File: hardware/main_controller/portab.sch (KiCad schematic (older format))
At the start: 2 parts

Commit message: Peripherals
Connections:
- net SPI_SCK: now reaches U?.30 (PA5/ADC1_IN5/ADC2_IN5/DAC_OUT2/SPI1_SCK/TIM2_CH1/TIM2_ETR/TIM8_CH1N/USB_OTG_HS_ULPI_CK)
- net SPI_MISO: now reaches U?.31 (PA6/ADC1_IN6/ADC2_IN6/DCMI_PIXCK/SPI1_MISO/TIM13_CH1/TIM1_BKIN/TIM3_CH1/TIM8_BKIN)
- net SPI_MOSI: now reaches U?.32 (PA7/ADC1_IN7/ADC2_IN7/ETH_CRS_DV/ETH_RX_DV/SPI1_MOSI/TIM14_CH1/TIM1_CH1N/TIM3_CH2/TIM8_CH1N)
- net I2C_SCL: now reaches U?.92 (PB6/CAN2_TX/DCMI_D5/I2C1_SCL/TIM4_CH1/USART1_TX)
- net I2C_SDA: now reaches U?.93 (PB7/DCMI_VSYNC/FSMC_NL/I2C1_SDA/TIM4_CH2/USART1_RX)
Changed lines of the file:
@@
 	1    0    0    -1
 $EndComp
-Wire Wire Line
-	6100 2300 7000 2300
-Wire Wire Line
-	6100 2400 7000 2400
-Text GLabel 7000 2300 2    50   Input ~ 0
+Text GLabel 6500 2300 2    50   Input ~ 0
 STM_DM
-Text GLabel 7000 2400 2    50   Input ~ 0
+Text GLabel 6500 2400 2    50   Input ~ 0
 STM_DP
 $Comp
@@
 Text GLabel 6800 3450 2    50   Input ~ 0
 BOOT1
+Wire Wire Line
+	6300 3850 6800 3850
+Wire Wire Line
+	6300 3950 6800 3950
+Text GLabel 6800 3850 2    50   Input ~ 0
+I2C_SCL
+Text GLabel 6800 3950 2    50   Input ~ 0
+I2C_SDA
+Wire Wire Line
+	6100 1700 6500 1700
+Wire Wire Line
+	6100 1800 6500 1800
+Wire Wire Line
+	6500 1900 6100 1900
+Text GLabel 6500 1700 2    50   Input ~ 0
+SPI_SCK
+Text GLabel 6500 1800 2    50   Input ~ 0
+SPI_MISO
+Text GLabel 6500 1900 2    50   Input ~ 0
+SPI_MOSI
+Wire Wire Line
+	6500 2300 6100 2300
+Wire Wire Line
+	6100 2400 6500 2400
 $EndSCHEMATC

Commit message: LEDs
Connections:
- net LED1: now reaches U?.23 (PA0-WKUP/ADC1_IN0/ADC2_IN0/ADC3_IN0/ETH_CRS/SYS_WKUP/TIM2_CH1/TIM2_ETR/TIM5_CH1/TIM8_ETR/UART4_TX/USART2_CTS)
- net LED2: now reaches U?.24 (PA1/ADC1_IN1/ADC2_IN1/ADC3_IN1/ETH_REF_CLK/ETH_RX_CLK/TIM2_CH2/TIM5_CH2/UART4_RX/USART2_RTS)
- net LED3: now reaches U?.25 (PA2/ADC1_IN2/ADC2_IN2/ADC3_IN2/ETH_MDIO/TIM2_CH3/TIM5_CH3/TIM9_CH1/USART2_TX)
- net LED4: now reaches U?.26 (PA3/ADC1_IN3/ADC2_IN3/ADC3_IN3/ETH_COL/TIM2_CH4/TIM5_CH4/TIM9_CH2/USART2_RX/USB_OTG_HS_ULPI_D0)
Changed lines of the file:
@@
 Wire Wire Line
 	6100 2400 6500 2400
+Wire Wire Line
+	6100 1200 6500 1200
+Wire Wire Line
+	6100 1300 6500 1300
+Wire Wire Line
+	6100 1400 6500 1400
+Wire Wire Line
+	6100 1500 6500 1500
+Text GLabel 6500 1200 2    50   Input ~ 0
+LED1
+Text GLabel 6500 1300 2    50   Input ~ 0
+LED2
+Text GLabel 6500 1400 2    50   Input ~ 0
+LED3
+Text GLabel 6500 1500 2    50   Input ~ 0
+LED4
 $EndSCHEMATC

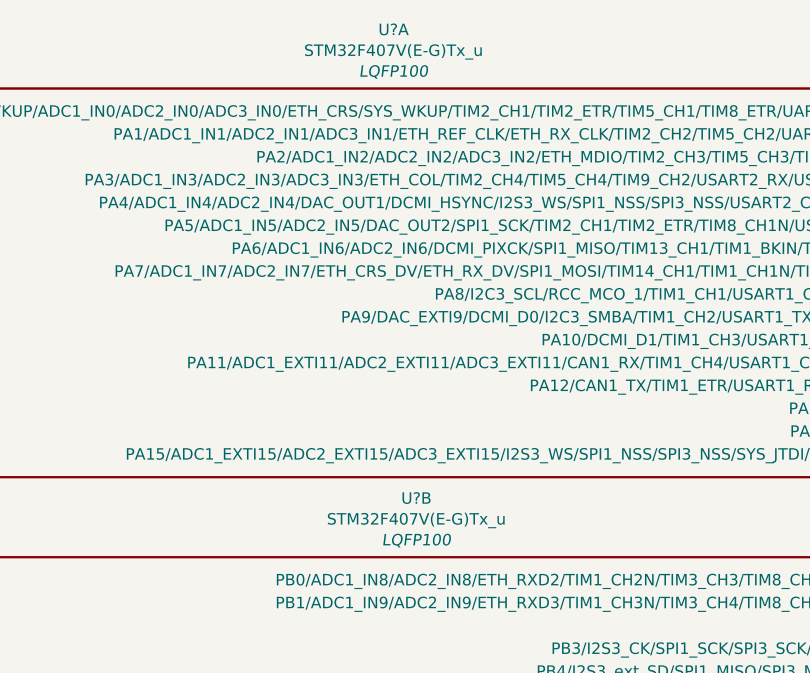
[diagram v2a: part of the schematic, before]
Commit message: Assigned names
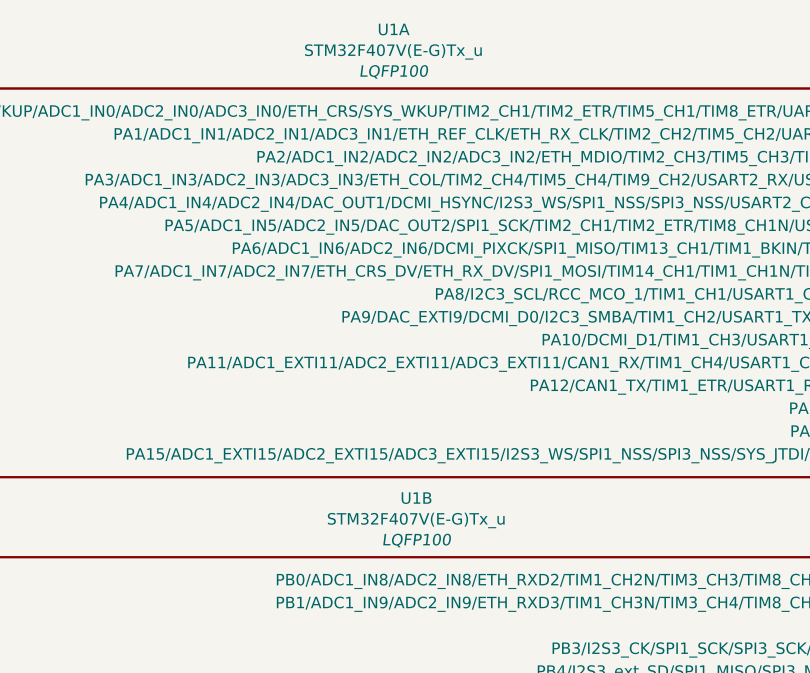
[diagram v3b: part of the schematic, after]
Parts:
- gave numbers to parts that had none: 1
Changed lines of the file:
@@
 $EndDescr
 $Comp
-L stm32:STM32F407V(E-G)Tx_u U?
+L stm32:STM32F407V(E-G)Tx_u U1
 U 1 1 5FD508FB
 P 3300 2000
-F 0 "U?" H 3232 3157 50  0000 C CNN
+F 0 "U1" H 3232 3157 50  0000 C CNN
 F 1 "STM32F407V(E-G)Tx_u" H 3232 3066 50  0000 C CNN
 F 2 "LQFP100" H 3232 2975 50  0000 C CIN
@@
 STM_DP
 $Comp
-L stm32:STM32F407V(E-G)Tx_u U?
+L stm32:STM32F407V(E-G)Tx_u U1
 U 2 1 5FD5951E
 P 3400 4050
-F 0 "U?" H 3332 5207 50  0000 C CNN
+F 0 "U1" H 3332 5207 50  0000 C CNN
 F 1 "STM32F407V(E-G)Tx_u" H 3332 5116 50  0000 C CNN
 F 2 "LQFP100" H 3332 5025 50  0000 C CIN

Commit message: usb protection
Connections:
- net VBUS_DETECT: now reaches U1.68 (PA9/DAC_EXTI9/DCMI_D0/I2C3_SMBA/TIM1_CH2/USART1_TX/USB_OTG_FS_VBUS)
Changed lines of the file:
@@
 Text GLabel 6500 1500 2    50   Input ~ 0
 LED4
+Wire Wire Line
+	6100 2100 6500 2100
+Text GLabel 6500 2100 2    50   Input ~ 0
+VBUS_DETECT
 $EndSCHEMATC

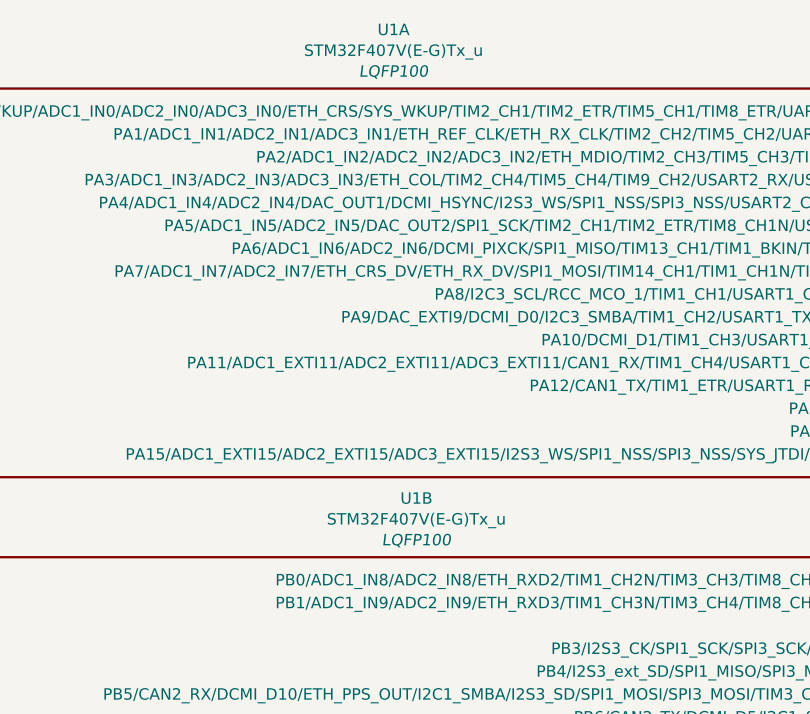
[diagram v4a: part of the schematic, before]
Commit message: assigned footprints
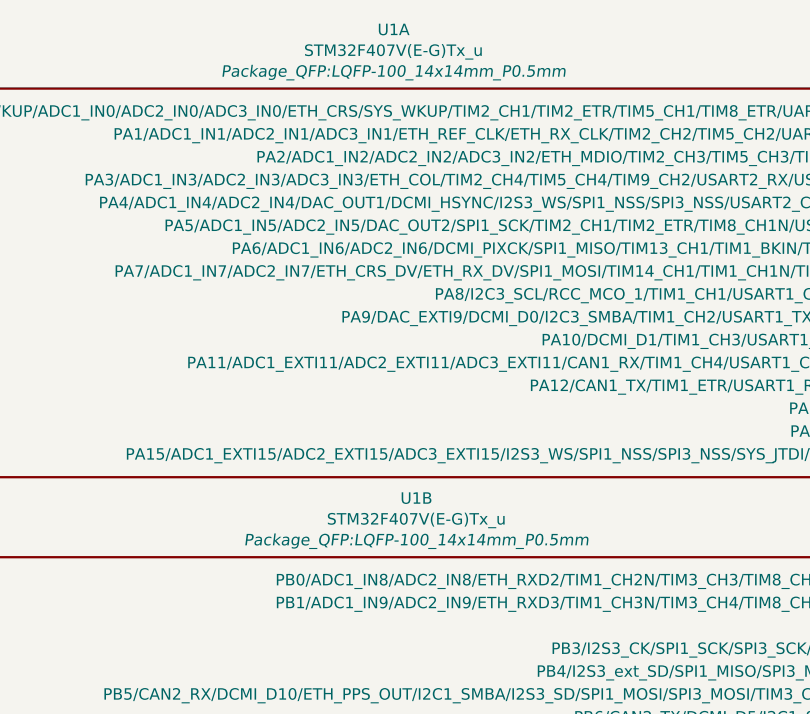
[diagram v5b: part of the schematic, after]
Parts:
- U1: footprint LQFP100 -> Package_QFP:LQFP-100_14x14mm_P0.5mm
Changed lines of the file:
@@
 F 0 "U1" H 3232 3157 50  0000 C CNN
 F 1 "STM32F407V(E-G)Tx_u" H 3232 3066 50  0000 C CNN
-F 2 "LQFP100" H 3232 2975 50  0000 C CIN
+F 2 "Package_QFP:LQFP-100_14x14mm_P0.5mm" H 3232 2975 50  0000 C CIN
 F 3 "" H 3300 2000 50  0000 C CNN
 	1    3300 2000
@@
 F 0 "U1" H 3332 5207 50  0000 C CNN
 F 1 "STM32F407V(E-G)Tx_u" H 3332 5116 50  0000 C CNN
-F 2 "LQFP100" H 3332 5025 50  0000 C CIN
+F 2 "Package_QFP:LQFP-100_14x14mm_P0.5mm" H 3332 5025 50  0000 C CIN
 F 3 "" H 3400 4050 50  0000 C CNN
 	2    3400 4050
